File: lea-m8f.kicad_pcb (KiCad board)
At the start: 2 copper layers, 33 parts, among them CON1 USB-MICRO-B, J1 RF_IN, J3 PPS, J4 30.72, P1 CONN_01X08, P2 5V IN, U1 NC7SZ125, U100 B200_GPSDO, U2 LT1962, U3 LEA-M8F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

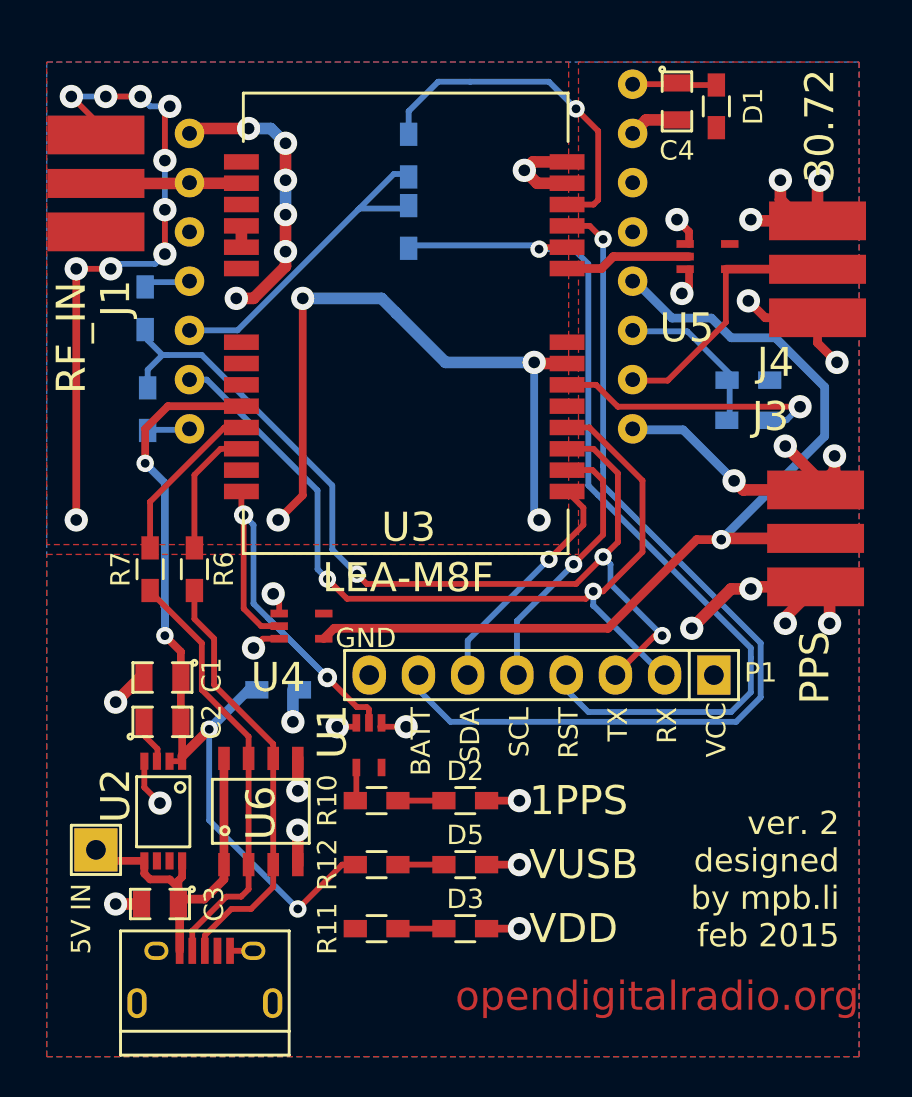
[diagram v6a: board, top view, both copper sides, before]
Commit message: Add more GND vias and move some tracks
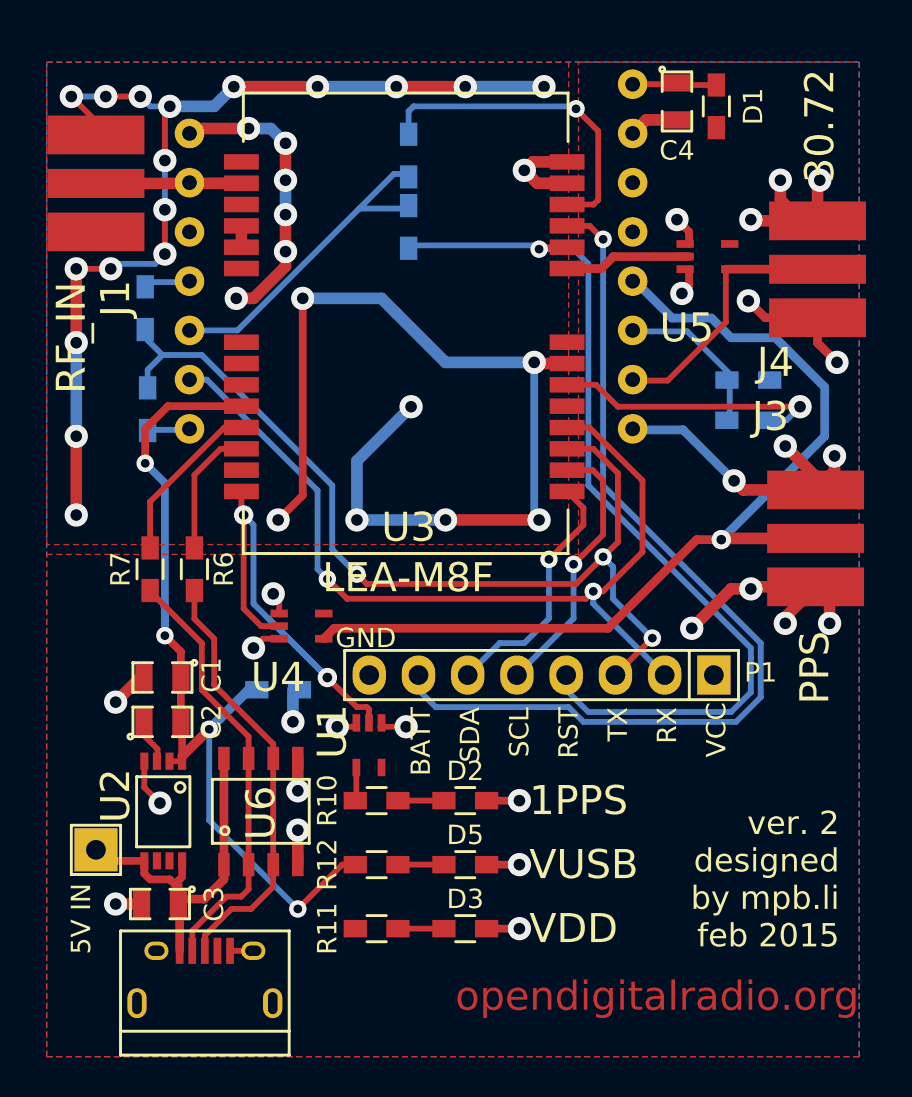
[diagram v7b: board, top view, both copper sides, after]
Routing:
- net GND: track 157.9 -> 193.8 mm, vias 47 -> 57
- net /SB_N: track 18.1 -> 17.0 mm
- net /SDA: track 12.3 -> 13.0 mm
- net /RXD: track 46.7 -> 46.0 mm
- net /TXD: track 50.1 -> 49.5 mm

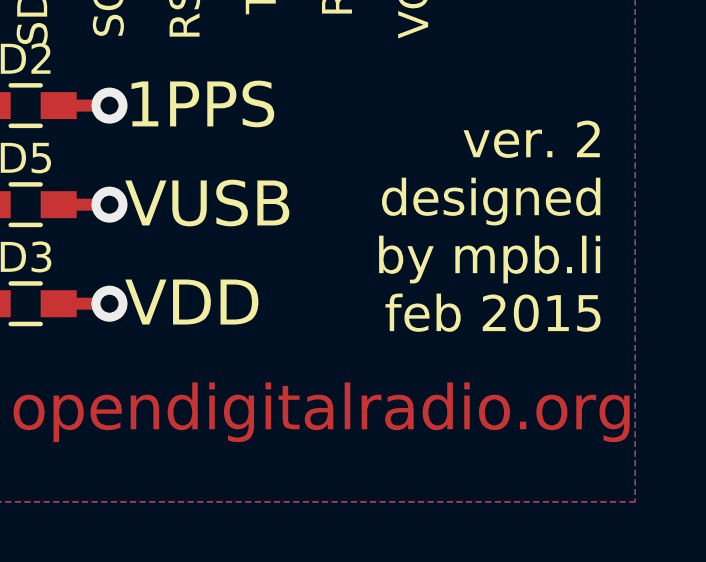
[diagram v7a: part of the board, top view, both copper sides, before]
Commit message: Some corrections, and change date on silkscreen
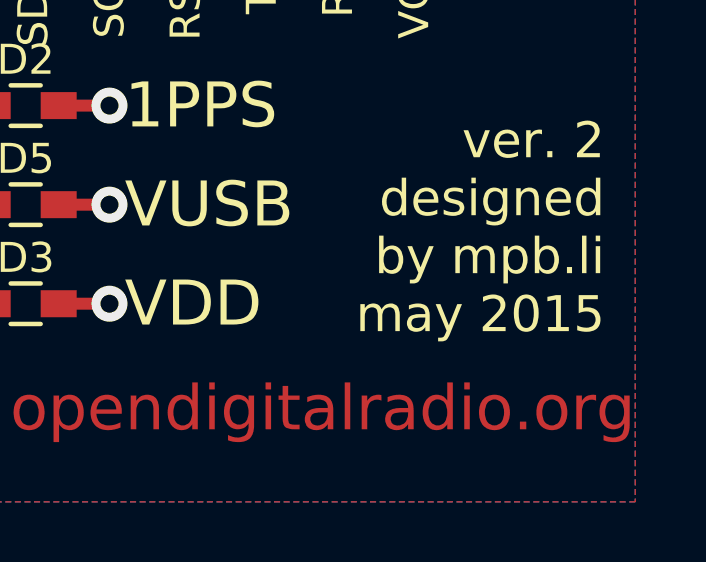
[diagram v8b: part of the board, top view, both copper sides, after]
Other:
- board text added: "ver. 2 designed by mpb.li may 2015"
- board text removed: "ver. 2 designed by mpb.li feb 2015"
